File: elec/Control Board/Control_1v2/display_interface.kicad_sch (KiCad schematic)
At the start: 20 parts, among them J35 Conn_02x05_Odd_Even, J36 Conn_02x05_Odd_Even, J801 Conn_01x03_0.1", J802 Con_01x02_0.1", J803 Screw_Terminal_01x04_5.08mm, J804 Screw_Terminal_01x02_5.08mm, J805 Con_01x02_0.1", K801 Relay SRU-12VDC, Q601 BSS138

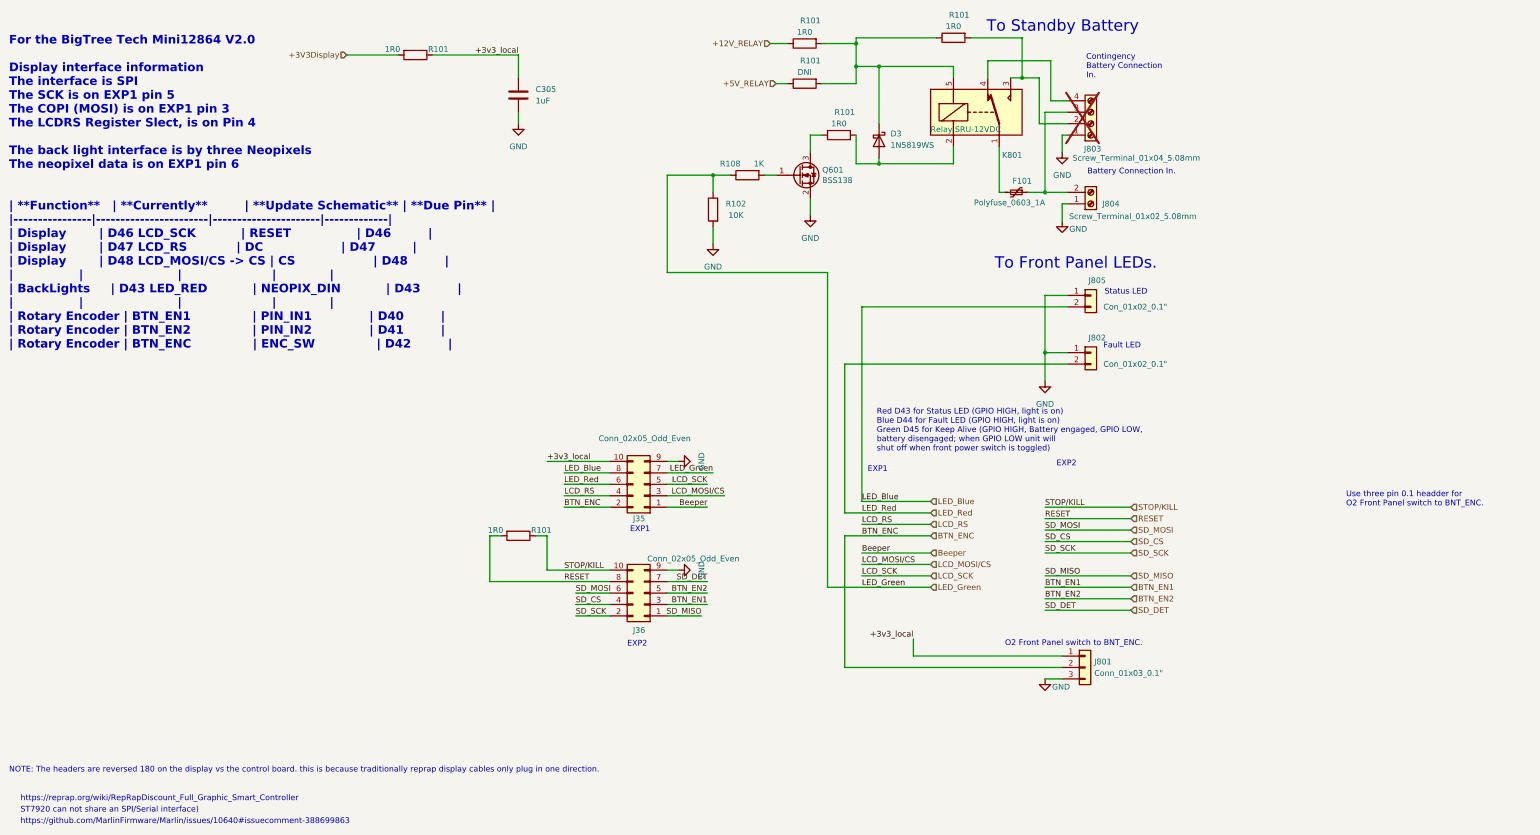
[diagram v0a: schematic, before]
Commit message: PCB V1.2. Initial route done.
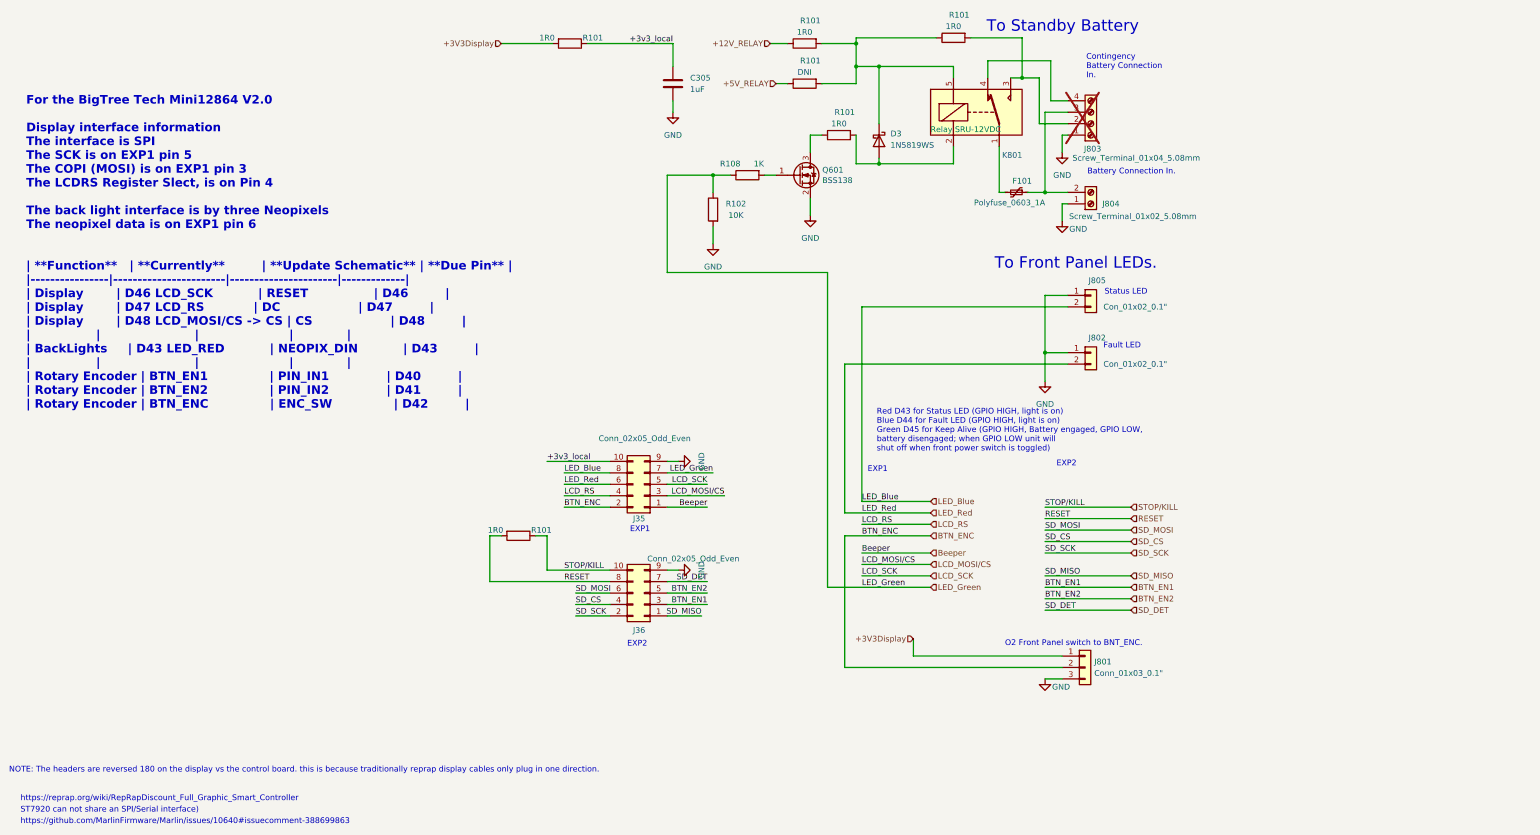
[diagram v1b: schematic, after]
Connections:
- net +3V3Display: now also J801.1 (Pin_1)
- net +3v3_local: no longer J801.1 (Pin_1)
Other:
- note removed: "Use three pin 0.1 headder for O2 Front Panel switch to BNT_ENC."
- moved on the sheet: C305, R101
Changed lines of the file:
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@@
     (stroke (width 0) (type default))
   )
-  (wire (pts (xy 93.98 22.86) (xy 105.41 22.86))
+  (wire (pts (xy 128.27 20.32) (xy 139.7 20.32))
     (stroke (width 0) (type default))
   )
@@
     (stroke (width 0) (type default))
   )
-  (wire (pts (xy 132.08 35.56) (xy 132.08 38.1))
+  (wire (pts (xy 166.37 33.02) (xy 166.37 35.56))
     (stroke (width 0) (type default))
   )
@@
     (stroke (width 0) (type default))
   )
-  (wire (pts (xy 113.03 22.86) (xy 132.08 22.86))
+  (wire (pts (xy 147.32 20.32) (xy 166.37 20.32))
     (stroke (width 0) (type default))
   )
@@
     (stroke (width 0) (type default))
   )
-  (wire (pts (xy 132.08 22.86) (xy 132.08 27.94))
+  (wire (pts (xy 166.37 20.32) (xy 166.37 25.4))
     (stroke (width 0) (type default))
   )
@@
     (stroke (width 0) (type default))
   )
-  (image (at 40.005 116.84)
+  (image (at 59.055 148.59)
     (data
       iVBORw0KGgoAAAANSUhEUgAAAZAAAAHaCAIAAAChHoiRAAAAA3NCSVQICAjb4U/gAAAgAElEQVR4
@@
   )
   (text "For the BigTree Tech Mini12864 V2.0\n\nDisplay interface information\nThe interface is SPI\nThe SCK is on EXP1 pin 5\nThe COPI (MOSI) is on EXP1 pin 3\nThe LCDRS Register Slect, is on Pin 4\n\nThe back light interface is by three Neopixels\nThe neopixel data is on EXP1 pin 6\n\n\n| **Function**   | **Currently**         | **Update Schematic** | **Due Pin** |\n|----------------|-----------------------|----------------------|-------------|\n| Display        | D46 LCD_SCK           | RESET                | D46         |\n| Display        | D47 LCD_RS            | DC                   | D47         |\n| Display        | D48 LCD_MOSI/CS -> CS | CS                   | D48         |\n|                |                       |                      |             |\n| BackLights     | D43 LED_RED           | NEOPIX_DIN           | D43         |\n|                |                       |                      |             |\n| Rotary Encoder | BTN_EN1               | PIN_IN1              | D40         |\n| Rotary Encoder | BTN_EN2               | PIN_IN2              | D41         |\n| Rotary Encoder | BTN_ENC               | ENC_SW               | D42         |"
-    (at 19.05 88.265 0)
+    (at 22.86 101.6 0)
     (effects (font (face "Courier New") (size 1.905 1.905) (thickness 0.381) bold) (justify left bottom))
   )
@@
     (effects (font (size 1.27 1.27)) (justify left bottom))
   )
-  (text "Use three pin 0.1 headder for \nO2 Front Panel switch to BNT_ENC."
-    (at 315.722 123.19 0)
-    (effects (font (size 1.27 1.27)) (justify left bottom))
-  )
   (text "To Standby Battery" (at 235.966 18.034 0)
     (effects (font (size 2.54 2.54)) (justify left bottom))
@@
     (effects (font (size 1.27 1.27)) (justify left bottom))
   )
-  (label "+3v3_local" (at 219.71 152.4 180) (fields_autoplaced)
-    (effects (font (size 1.27 1.27)) (justify right bottom))
-  )
   (label "SD_MISO" (at 172.72 147.32 180) (fields_autoplaced)
     (effects (font (size 1.27 1.27)) (justify right bottom))
@@
     (effects (font (size 1.27 1.27)) (justify left bottom))
   )
-  (label "+3v3_local" (at 132.08 22.86 180) (fields_autoplaced)
+  (label "+3v3_local" (at 166.37 20.32 180) (fields_autoplaced)
     (effects (font (size 1.27 1.27)) (justify right bottom))
   )
@@
     (effects (font (size 1.27 1.27)) (justify left))
   )
-  (hierarchical_label "+3V3Display" (shape input) (at 93.98 22.86 180) (fields_autoplaced)
+  (hierarchical_label "+3V3Display" (shape input) (at 128.27 20.32 180) (fields_autoplaced)
     (effects (font (size 1.27 1.27)) (justify right))
   )
@@
     (effects (font (size 1.27 1.27)) (justify left))
   )
+  (hierarchical_label "+3V3Display" (shape input) (at 219.71 152.4 180) (fields_autoplaced)
+    (effects (font (size 1.27 1.27)) (justify right))
+  )
   (symbol (lib_id "Connector_Generic:Conn_01x02") (at 259.08 76.2 0) (unit 1)
     (in_bom yes) (on_board yes) (dnp no)
@@
     )
   )
-  (symbol (lib_id "Device:C") (at 132.08 31.75 0) (unit 1)
+  (symbol (lib_id "Device:C") (at 166.37 29.21 0) (unit 1)
     (in_bom yes) (on_board yes) (dnp no) (fields_autoplaced)
-    (property "Reference" "C305" (at 135.89 30.4799 0)
+    (property "Reference" "C305" (at 170.18 27.9399 0)
       (effects (font (size 1.27 1.27)) (justify left))
     )
-    (property "Value" "1uF" (at 135.89 33.0199 0)
+    (property "Value" "1uF" (at 170.18 30.4799 0)
       (effects (font (size 1.27 1.27)) (justify left))
     )
-    (property "Footprint" "Capacitor_SMD:C_0603_1608Metric_Pad1.08x0.95mm_HandSolder" (at 133.0452 35.56 0)
+    (property "Footprint" "Capacitor_SMD:C_0603_1608Metric_Pad1.08x0.95mm_HandSolder" (at 167.3352 33.02 0)
       (effects (font (size 1.27 1.27)) hide)
     )
-    (property "Datasheet" "CC0603JRX7R9BB104.pdf" (at 132.08 31.75 0)
+    (property "Datasheet" "CC0603JRX7R9BB104.pdf" (at 166.37 29.21 0)
       (effects (font (size 1.27 1.27)) hide)
     )
-    (property "AssemblyType" "SMT" (at 132.08 31.75 0)
+    (property "AssemblyType" "SMT" (at 166.37 29.21 0)
       (effects (font (size 1.27 1.27)) hide)
     )
-    (property "Distributor 1" "JLCPCB" (at 132.08 31.75 0)
+    (property "Distributor 1" "JLCPCB" (at 166.37 29.21 0)
       (effects (font (size 1.27 1.27)) hide)
     )
-    (property "Distributor 1 PN" "C91183" (at 132.08 31.75 0)
+    (property "Distributor 1 PN" "C91183" (at 166.37 29.21 0)
       (effects (font (size 1.27 1.27)) hide)
     )
-    (property "Cost" "0.0037" (at 132.08 31.75 0)
+    (property "Cost" "0.0037" (at 166.37 29.21 0)
       (effects (font (size 1.27 1.27)) hide)
     )
-    (property "MPN" "CC0603JRX7R9BB104" (at 132.08 31.75 0)
+    (property "MPN" "CC0603JRX7R9BB104" (at 166.37 29.21 0)
       (effects (font (size 1.27 1.27)) hide)
     )
-    (property "Manufacturer" "YAGEO" (at 132.08 31.75 0)
+    (property "Manufacturer" "YAGEO" (at 166.37 29.21 0)
       (effects (font (size 1.27 1.27)) hide)
     )
-    (property "LongLead" "NO" (at 132.08 31.75 0)
+    (property "LongLead" "NO" (at 166.37 29.21 0)
       (effects (font (size 1.27 1.27)) hide)
     )
-    (property "Description" "50V 1uF ±5% 0603 Multilayer Ceramic Ca" (at 132.08 31.75 0)
+    (property "Description" "50V 1uF ±5% 0603 Multilayer Ceramic Ca" (at 166.37 29.21 0)
       (effects (font (size 1.27 1.27)) hide)
     )
@@
     )
   )
-  (symbol (lib_name "GND_5") (lib_id "power:GND") (at 132.08 38.1 0) (unit 1)
+  (symbol (lib_name "GND_5") (lib_id "power:GND") (at 166.37 35.56 0) (unit 1)
     (in_bom yes) (on_board yes) (dnp no) (fields_autoplaced)
-    (property "Reference" "#PWR0307" (at 132.08 44.45 0)
+    (property "Reference" "#PWR0307" (at 166.37 41.91 0)
       (effects (font (size 1.27 1.27)) hide)
     )
-    (property "Value" "GND" (at 132.08 43.18 0)
+    (property "Value" "GND" (at 166.37 40.64 0)
       (effects (font (size 1.27 1.27)))
     )
-    (property "Footprint" "" (at 132.08 38.1 0)
+    (property "Footprint" "" (at 166.37 35.56 0)
       (effects (font (size 1.27 1.27)) hide)
     )
-    (property "Datasheet" "" (at 132.08 38.1 0)
+    (property "Datasheet" "" (at 166.37 35.56 0)
       (effects (font (size 1.27 1.27)) hide)
     )
@@
     )
   )
-  (symbol (lib_id "Device:R") (at 109.22 22.86 270) (unit 1)
+  (symbol (lib_id "Device:R") (at 143.51 20.32 270) (unit 1)
     (in_bom yes) (on_board yes) (dnp no)
-    (property "Reference" "R101" (at 114.3 21.59 90)
+    (property "Reference" "R101" (at 148.59 19.05 90)
       (effects (font (size 1.27 1.27)))
     )
-    (property "Value" "1R0" (at 104.14 21.59 90)
+    (property "Value" "1R0" (at 138.43 19.05 90)
       (effects (font (size 1.27 1.27)))
     )
-    (property "Footprint" "Resistor_SMD:R_0603_1608Metric_Pad0.98x0.95mm_HandSolder" (at 109.22 21.082 90)
+    (property "Footprint" "Resistor_SMD:R_0603_1608Metric_Pad0.98x0.95mm_HandSolder" (at 143.51 18.542 90)
       (effects (font (size 1.27 1.27)) hide)
     )
-    (property "Datasheet" "~" (at 109.22 22.86 0)
+    (property "Datasheet" "~" (at 143.51 20.32 0)
       (effects (font (size 1.27 1.27)) hide)
     )
-    (property "Distributor 1" "JLCPCB" (at 109.22 22.86 90)
+    (property "Distributor 1" "JLCPCB" (at 143.51 20.32 90)
       (effects (font (size 1.27 1.27)) hide)
     )
-    (property "Distributor 1 PN" "C269434" (at 109.22 22.86 90)
+    (property "Distributor 1 PN" "C269434" (at 143.51 20.32 90)
       (effects (font (size 1.27 1.27)) hide)
     )
-    (property "Manufacturer" "TyoHM" (at 109.22 22.86 90)
+    (property "Manufacturer" "TyoHM" (at 143.51 20.32 90)
       (effects (font (size 1.27 1.27)) hide)
     )
-    (property "MPN" "RMC060315%N" (at 109.22 22.86 90)
+    (property "MPN" "RMC060315%N" (at 143.51 20.32 90)
       (effects (font (size 1.27 1.27)) hide)
     )
-    (property "Description" "0.1W ±5% 1Ω 0603 Chip Resistor - Surface Mount ROHS" (at 109.22 22.86 0)
+    (property "Description" "0.1W ±5% 1Ω 0603 Chip Resistor - Surface Mount ROHS" (at 143.51 20.32 0)
       (effects (font (size 1.27 1.27)) hide)
     )
-    (property "AssemblyType" "SMT" (at 109.22 22.86 0)
+    (property "AssemblyType" "SMT" (at 143.51 20.32 0)
       (effects (font (size 1.27 1.27)) hide)
     )
-    (property "Cost" "0.0015" (at 109.22 22.86 0)
+    (property "Cost" "0.0015" (at 143.51 20.32 0)
       (effects (font (size 1.27 1.27)) hide)
     )
-    (property "LongLead" "NO" (at 109.22 22.86 0)
+    (property "LongLead" "NO" (at 143.51 20.32 0)
       (effects (font (size 1.27 1.27)) hide)
     )

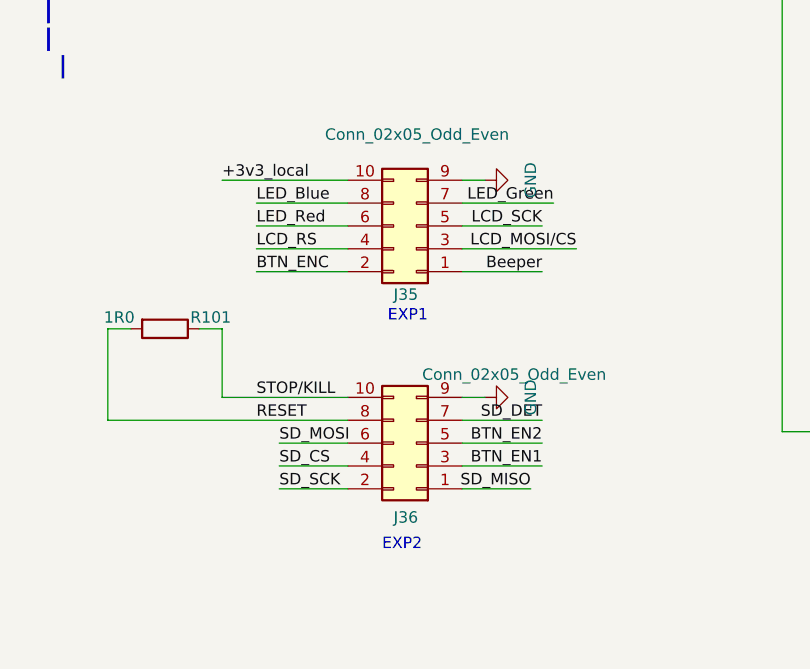
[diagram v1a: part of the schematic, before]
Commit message: PCB V1.2. Update with footprint JST_PUD_B24B-PUDSS_2x12_P2.00mm_Vertical with STEP file.
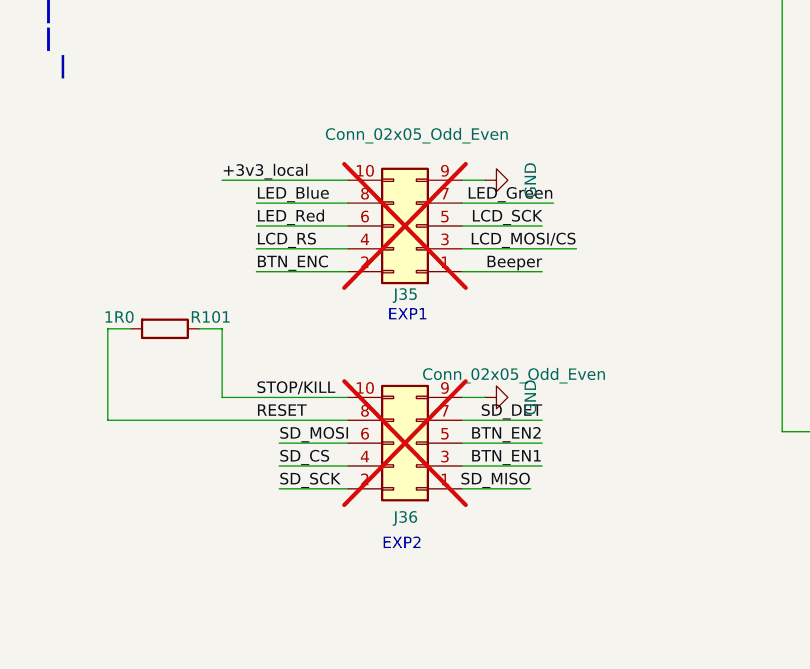
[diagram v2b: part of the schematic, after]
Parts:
- J35, J36: now not fitted; now left out of the parts list
- J803: now left out of the parts list
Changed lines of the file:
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@@
   )
   (symbol (lib_id "Connector_Generic:Conn_02x05_Odd_Even") (at 160.02 142.24 180) (unit 1)
-    (in_bom yes) (on_board yes) (dnp no)
+    (in_bom no) (on_board yes) (dnp yes)
     (property "Reference" "J36" (at 157.48 150.495 0)
       (effects (font (size 1.27 1.27)) (justify right))
@@
   )
   (symbol (lib_id "Connector:Screw_Terminal_01x04") (at 259.08 38.1 0) (mirror x) (unit 1)
-    (in_bom yes) (on_board yes) (dnp yes)
+    (in_bom no) (on_board yes) (dnp yes)
     (property "Reference" "J803" (at 257.556 43.688 0)
       (effects (font (size 1.27 1.27)) (justify left))
@@
   )
   (symbol (lib_id "Connector_Generic:Conn_02x05_Odd_Even") (at 160.02 118.11 180) (unit 1)
-    (in_bom yes) (on_board yes) (dnp no)
+    (in_bom no) (on_board yes) (dnp yes)
     (property "Reference" "J35" (at 157.48 125.73 0)
       (effects (font (size 1.27 1.27)) (justify right))

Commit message: PCB V1.2. Add part numbers for 5.08mm screw terminal.
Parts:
- J803: Cost 1000000 -> 2.65000; Distributor 1 (none) -> Digikey; Distributor 1 PN (none) -> 277-1265-ND; MPN (none) -> 1715747; Manufacturer (none) -> Phoenix Contact
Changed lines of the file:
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@@
       (effects (font (size 1.27 1.27)) hide)
     )
-    (property "Datasheet" "~" (at 259.08 38.1 0)
+    (property "Datasheet" "https://www.phoenixcontact.com/us/products/1715747/pdf" (at 259.08 38.1 0)
       (effects (font (size 1.27 1.27)) hide)
     )
-    (property "Cost" "1000000" (at 259.08 38.1 0)
+    (property "Cost" "2.65000" (at 259.08 38.1 0)
       (effects (font (size 1.27 1.27)) hide)
     )
-    (property "Description" "" (at 259.08 38.1 0)
+    (property "Description" "TERM BLK 4P SIDE ENT 5.08MM PCB" (at 259.08 38.1 0)
       (effects (font (size 1.27 1.27)) hide)
     )
-    (property "Distributor 1" "" (at 259.08 38.1 0)
+    (property "Distributor 1" "Digikey" (at 259.08 38.1 0)
       (effects (font (size 1.27 1.27)) hide)
     )
-    (property "Distributor 1 PN" "" (at 259.08 38.1 0)
+    (property "Distributor 1 PN" "277-1265-ND" (at 259.08 38.1 0)
       (effects (font (size 1.27 1.27)) hide)
     )
-    (property "MPN" "" (at 259.08 38.1 0)
+    (property "MPN" "1715747" (at 259.08 38.1 0)
       (effects (font (size 1.27 1.27)) hide)
     )
-    (property "Manufacturer" "" (at 259.08 38.1 0)
+    (property "Manufacturer" "Phoenix Contact" (at 259.08 38.1 0)
       (effects (font (size 1.27 1.27)) hide)
     )
